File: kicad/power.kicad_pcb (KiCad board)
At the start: 2 copper layers, 84.1 x 61.7 mm, 12 parts, among them J1 Bus_PCI_Express_x1, J2 Conn_01x02_Pin, J6 USB_C_Receptacle_USB2.0_16P

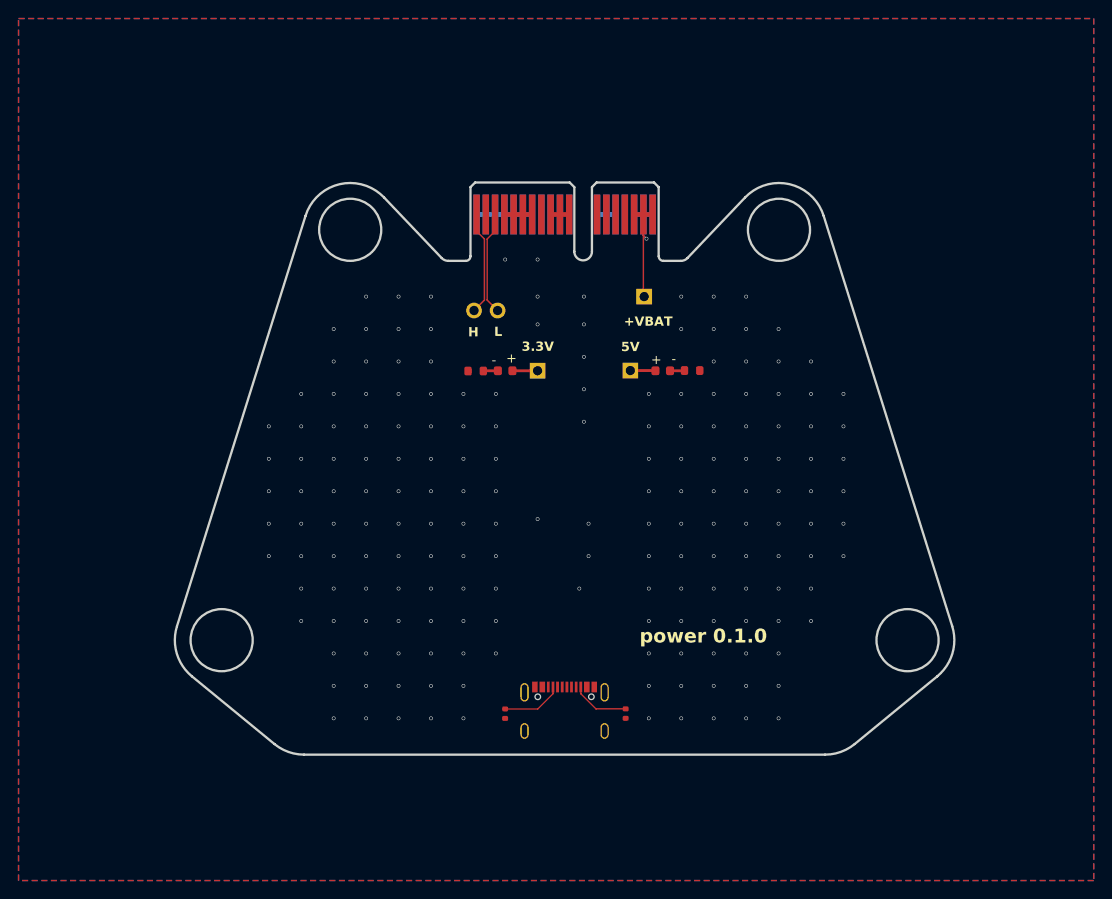
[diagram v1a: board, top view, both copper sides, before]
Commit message: Add MCU and CAN chips
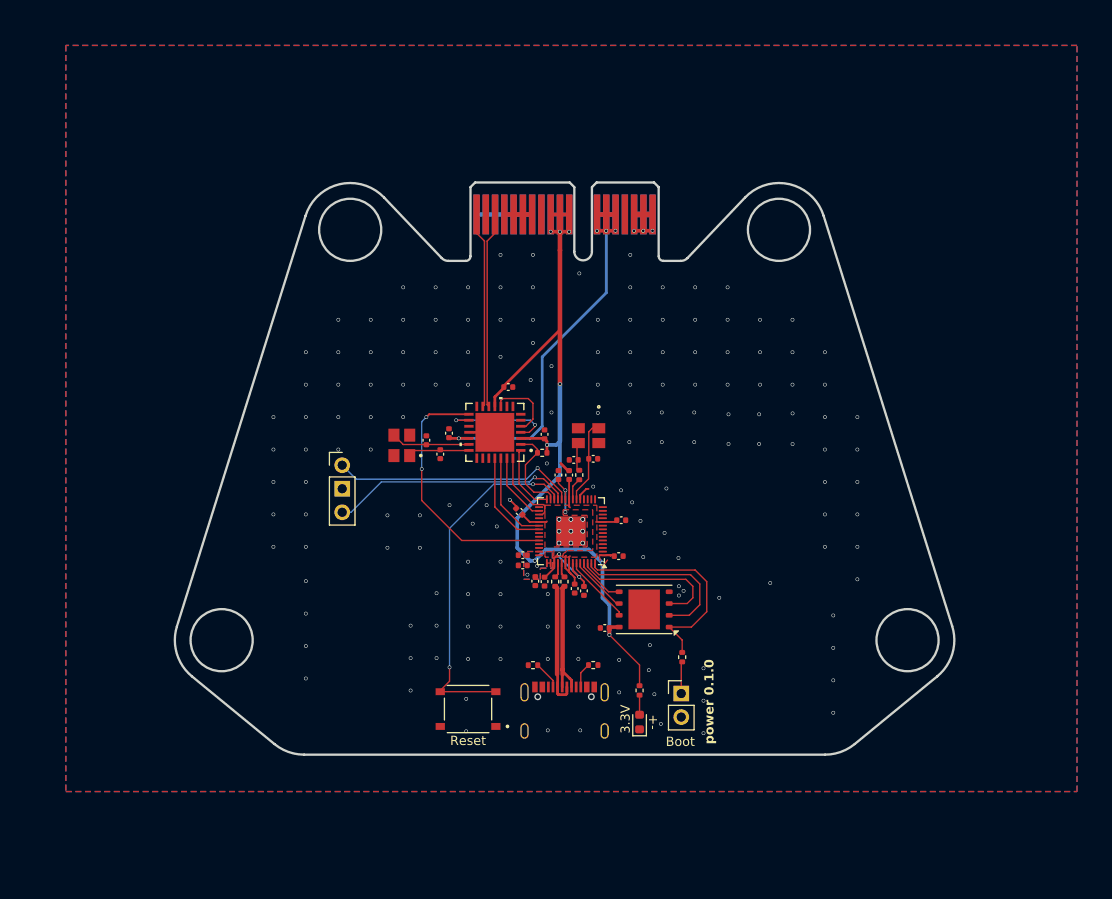
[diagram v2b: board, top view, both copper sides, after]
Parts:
- removed D1, D2: LED, LED_SMD:LED_0603_1608Metric
- removed J2: Conn_01x02_Pin, Connector_PinHeader_2.54mm:PinHeader_1x02_P2.54mm_Vertical
- removed R1, R2: 150, Resistor_SMD:R_0603_1608Metric
- removed TP1, TP2, TP3: TestPoint, Connector_PinHeader_2.54mm:PinHeader_1x01_P2.54mm_Vertical
- added C27: 15p, Capacitor_SMD:C_0402_1005Metric, F.Cu at (149.5, 90.5)
- added C28: 15p, Capacitor_SMD:C_0402_1005Metric, F.Cu at (147.4, 90.6)
- added C29: 100n, Capacitor_SMD:C_0402_1005Metric, F.Cu at (150.8, 108.8)
- added C30: 100n, Capacitor_SMD:C_0402_1005Metric, F.Cu at (140.3, 82.8)
- added C31: 22p, Capacitor_SMD:C_0402_1005Metric, F.Cu at (133.0, 90.0)
- added C32: 100n, Capacitor_SMD:C_0402_1005Metric, F.Cu at (144.2, 87.9)
- added C33: 22p, Capacitor_SMD:C_0402_1005Metric, F.Cu at (131.5, 88.5)
- added C34: 100n, Capacitor_SMD:C_0402_1005Metric, F.Cu at (133.9, 87.7)
- added C35: 100n, Capacitor_SMD:C_0402_1005Metric, F.Cu at (148.5, 104.8)
- added C36: 100n, Capacitor_SMD:C_0402_1005Metric, F.Cu at (145.8, 92.2)
- added C37: 1u, Capacitor_SMD:C_0402_1005Metric, F.Cu at (144.2, 103.8)
- added C38: 100n, Capacitor_SMD:C_0402_1005Metric, F.Cu at (147.5, 104.5)
- added C39: 1u, Capacitor_SMD:C_0402_1005Metric, F.Cu at (143.2, 103.7)
- added C40: 100n, Capacitor_SMD:C_0402_1005Metric, F.Cu at (152.2, 101.0)
- added C41: 100n, Capacitor_SMD:C_0402_1005Metric, F.Cu at (141.5, 96.2)
- added C42: 100n, Capacitor_SMD:C_0402_1005Metric, F.Cu at (152.5, 97.1)
- added C43: 100n, Capacitor_SMD:C_0402_1005Metric, F.Cu at (146.9, 92.3)
- added C44: 100n, Capacitor_SMD:C_0402_1005Metric, F.Cu at (141.9, 100.9)
- added C45: 100n, Capacitor_SMD:C_0402_1005Metric, F.Cu at (141.9, 102.0)
- added D5: LED, LED_SMD:LED_0603_1608Metric, F.Cu at (154.5, 118.9)
- added J3: Conn_01x03, Connector_PinHeader_2.54mm:PinHeader_1x03_P2.54mm_Vertical, F.Cu at (122.4, 91.2)
- added J5: Conn_01x02_Pin, Connector_PinHeader_2.54mm:PinHeader_1x02_P2.54mm_Vertical, F.Cu at (159.0, 115.8)
- added R25: 1k, Resistor_SMD:R_0402_1005Metric, F.Cu at (159.1, 111.9)
- added R26: 1k, Resistor_SMD:R_0402_1005Metric, F.Cu at (148.0, 92.2)
- added R29: 10k, Resistor_SMD:R_0402_1005Metric, F.Cu at (144.0, 89.9)
- added R30: 1 k, Resistor_SMD:R_0402_1005Metric, F.Cu at (154.5, 115.5)
- added R31: 27, Resistor_SMD:R_0402_1005Metric, F.Cu at (146.4, 103.8)
- added R32: 27, Resistor_SMD:R_0402_1005Metric, F.Cu at (145.4, 103.8)
- added S2: TS-1187A-B-A-B, 4in-kicad-library:TS-1187A-B-A-B, F.Cu at (136.0, 117.5)
- added U5: W25Q128JVP, Package_SON:WSON-8-1EP_6x5mm_P1.27mm_EP3.4x4.3mm, F.Cu at (155.0, 106.8)
- added U6: MCP25625T-E/ML, 4in-kicad-library:QFN28_6X6MC_MCH, F.Cu at (138.9, 87.6)
- added U7: RP2040, Package_DFN_QFN:QFN-56-1EP_7x7mm_P0.4mm_EP3.2x3.2mm, F.Cu at (147.1, 98.3)
- added X1: ABM8-272-T3, 4in-kicad-library:ABM8-272-T3_ABR, F.Cu at (149.0, 88.0)
- added Y1: X322516MLB4SI, 4in-kicad-library:X322516MLB4SI, F.Cu at (128.8, 89.1)
- moved R4 6.29 mm to (149.5, 112.8), turned to 0 degrees
- moved R3 6.04 mm to (143.0, 112.8), turned to 0 degrees
- renumbered J1 to J4
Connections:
- net +BAT renamed v_lipo
- J4 pad A1: CANP -> CANH
- J4 pad A3: CANN -> CANL
- J6 pad A1: GND -> LOAD_GND
- J6 pad A12: GND -> LOAD_GND
- J6 pad A4: +5V -> VIN
- J6 pad A9: +5V -> VIN
- J6 pad B1: GND -> LOAD_GND
- J6 pad B12: GND -> LOAD_GND
- J6 pad S1: GND -> LOAD_GND
- R3 pad 1: GND -> LOAD_GND
- R4 pad 2: GND -> LOAD_GND
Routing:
- net +3.3V: track 5.22 -> 112.4 mm, vias 0 -> 10
- net +5V: track 4.67 -> 43.2 mm, vias 0 -> 4
- net /RUN: track 0.00 -> 38.3 mm, vias 0 -> 2
- net (no net): track 0.00 -> 28.7 mm
- net CANSTBY: track 0.00 -> 28.4 mm, vias 0 -> 2
- net /SWCLK: track 0.00 -> 26.7 mm, vias 0 -> 1
- net /SWD: track 0.00 -> 26.2 mm, vias 0 -> 1
- net /QSPI_SS: track 0.00 -> 24.5 mm
- net CANH: track 0.00 -> 21.1 mm
- net CANL: track 0.00 -> 21.1 mm
- net /QSPI_SD1: track 0.00 -> 18.9 mm
- net /QSPI_SD2: track 0.00 -> 16.7 mm
- net +1.1V: track 0.00 -> 14.4 mm, vias 0 -> 4
- net v_lipo: track 18.4 -> 6.00 mm, vias 1 -> 3
- net tx: track 0.00 -> 12.1 mm, vias 0 -> 2
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- added copper zone on F.Cu, net +1.1V
- added copper zone on B.Cu, net +3.3V
- added copper zone on F.Cu, net +3.3V
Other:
- board text added: "+-"
- board text added: "Boot"
- board text added: "Reset"
- board text removed: "+VBAT"
- board text removed: "5V"
- board text removed: "H"
- board text removed: "L"

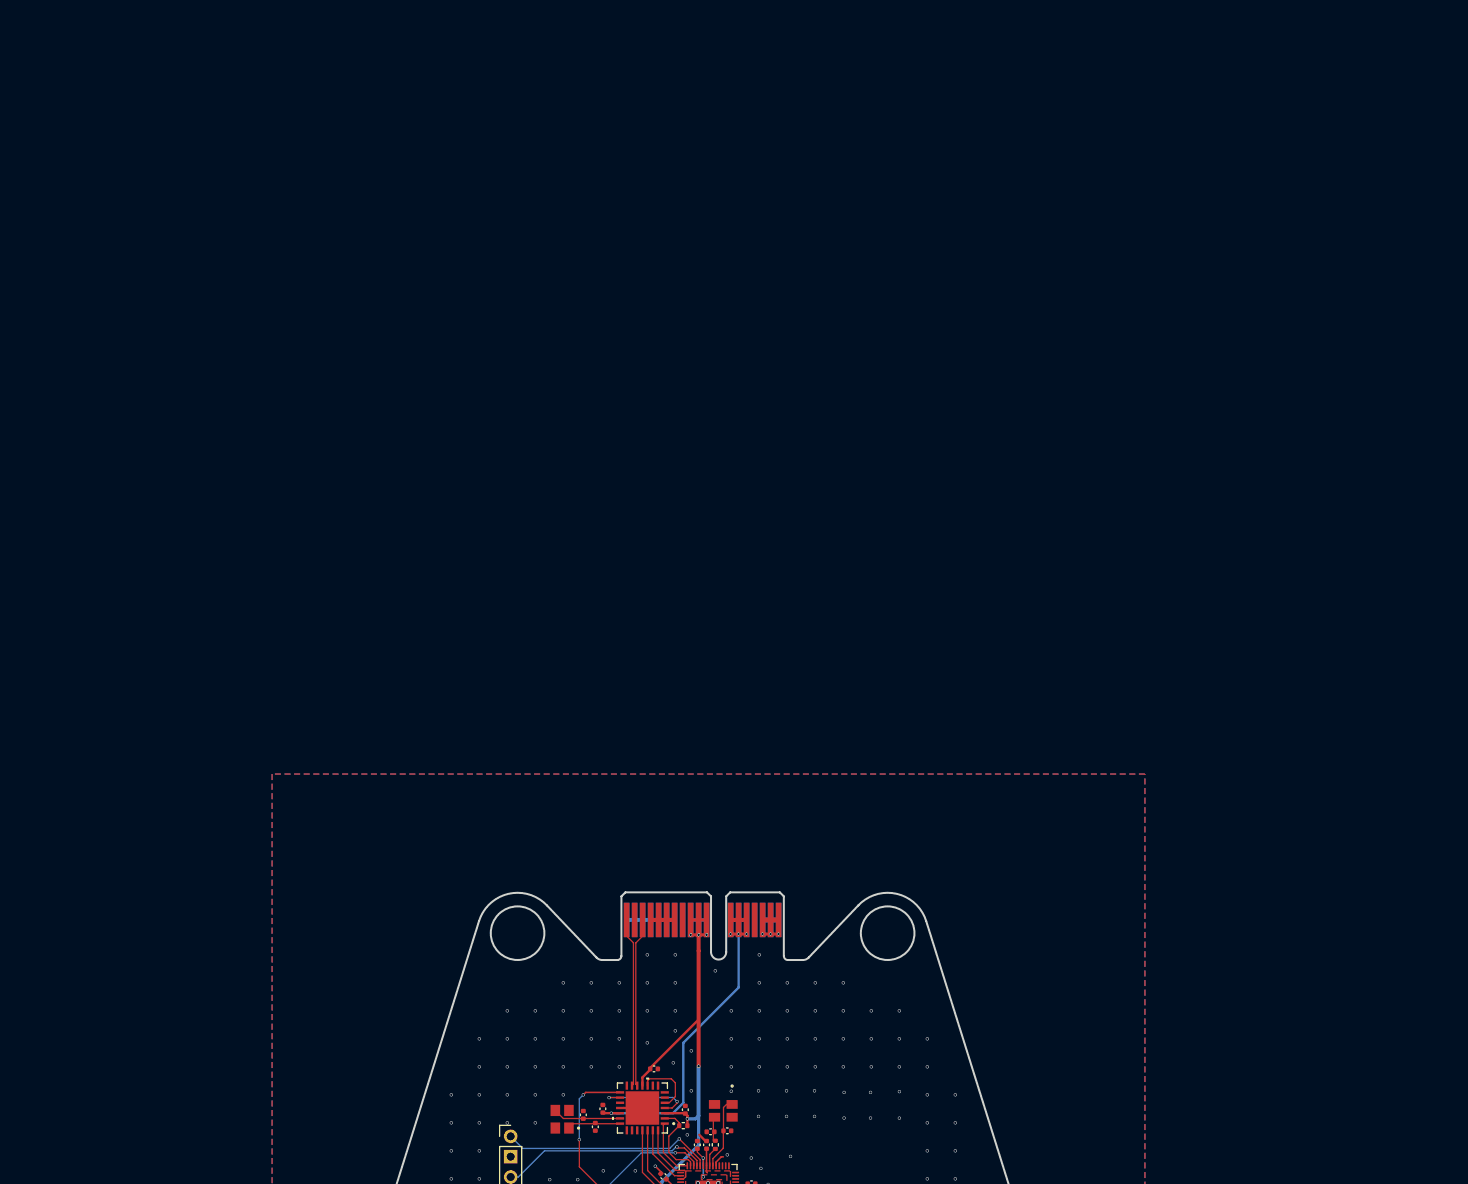
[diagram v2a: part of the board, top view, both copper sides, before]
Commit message: Update component placement
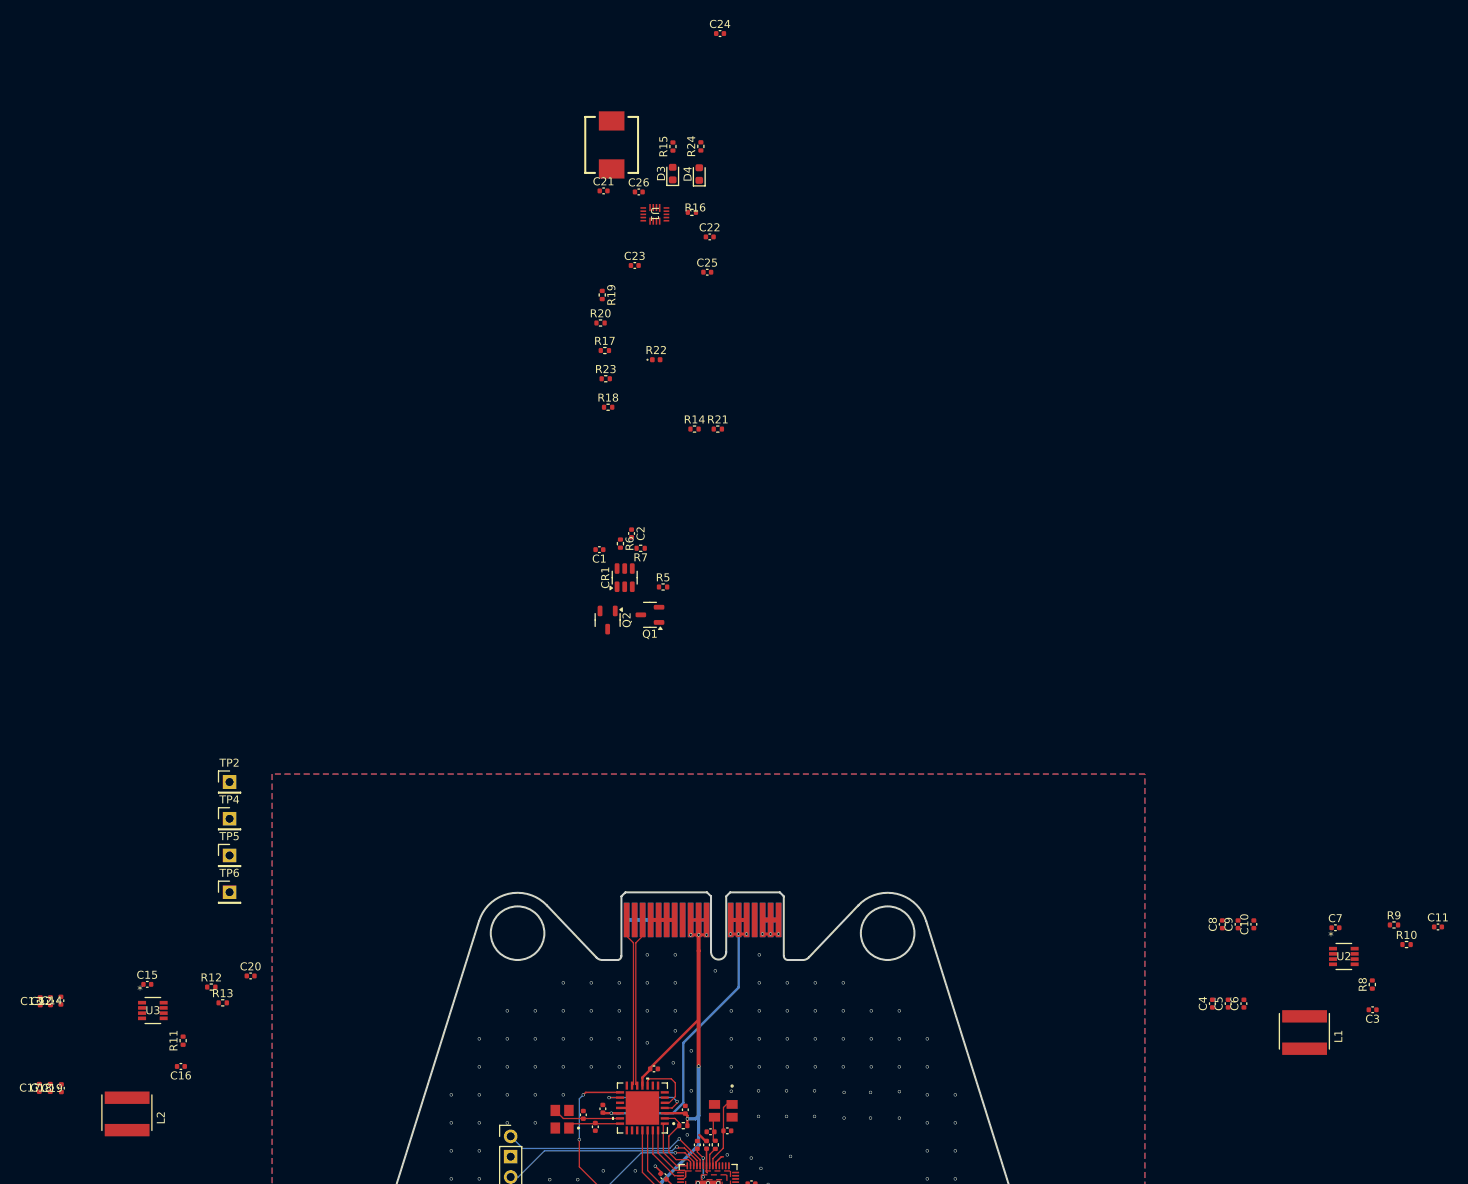
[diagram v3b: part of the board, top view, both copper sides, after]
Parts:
- added C1: 0.1u, Capacitor_SMD:C_0402_1005Metric, F.Cu at (133.5, 17.9)
- added C10: 22u, Capacitor_SMD:C_0402_1005Metric, F.Cu at (215.3, 64.7)
- added C11: 220p, Capacitor_SMD:C_0402_1005Metric, F.Cu at (238.3, 65.0)
- added C12: 22u, Capacitor_SMD:C_0402_1005Metric, F.Cu at (64.9, 74.3)
- added C13: 22u, Capacitor_SMD:C_0402_1005Metric, F.Cu at (63.6, 74.3)
- added C14: 1u, Capacitor_SMD:C_0402_1005Metric, F.Cu at (66.2, 74.2)
- added C15: 1u, Capacitor_SMD:C_0402_1005Metric, F.Cu at (77.0, 72.2)
- added C16: 0.1u, Capacitor_SMD:C_0402_1005Metric, F.Cu at (81.2, 82.5)
- added C17: 22u, Capacitor_SMD:C_0402_1005Metric, F.Cu at (63.5, 85.1)
- added C18: 22u, Capacitor_SMD:C_0402_1005Metric, F.Cu at (64.9, 85.1)
- added C19: 22u, Capacitor_SMD:C_0402_1005Metric, F.Cu at (66.3, 85.2)
- added C2: 0.1u, Capacitor_SMD:C_0402_1005Metric, F.Cu at (137.5, 15.8)
- added C20: 220p, Capacitor_SMD:C_0402_1005Metric, F.Cu at (89.9, 71.1)
- added C21: 10u, Capacitor_SMD:C_0402_1005Metric, F.Cu at (134.0, -27.0)
- added C22: 22u, Capacitor_SMD:C_0402_1005Metric, F.Cu at (147.3, -21.2)
- added C23: 1u, Capacitor_SMD:C_0402_1005Metric, F.Cu at (137.9, -17.7)
- added C24: 10u, Capacitor_SMD:C_0402_1005Metric, F.Cu at (148.6, -46.7)
- added C25: 22u, Capacitor_SMD:C_0402_1005Metric, F.Cu at (147.0, -16.8)
- added C26: 100n, Capacitor_SMD:C_0402_1005Metric, F.Cu at (138.4, -26.9)
- added C3: 0.1u, Capacitor_SMD:C_0402_1005Metric, F.Cu at (230.2, 75.4)
- added C4: 22u, Capacitor_SMD:C_0402_1005Metric, F.Cu at (210.1, 74.6)
- added C5: 22u, Capacitor_SMD:C_0402_1005Metric, F.Cu at (212.1, 74.6)
- added C6: 22u, Capacitor_SMD:C_0402_1005Metric, F.Cu at (214.1, 74.6)
- added C7: 1u, Capacitor_SMD:C_0402_1005Metric, F.Cu at (225.5, 65.1)
- added C8: 1u, Capacitor_SMD:C_0402_1005Metric, F.Cu at (211.4, 64.7)
- added C9: 22u, Capacitor_SMD:C_0402_1005Metric, F.Cu at (213.3, 64.7)
- added CR1: S-8252AAL-M6T1U, Package_TO_SOT_SMD:SOT-23-6, F.Cu at (136.7, 21.4)
- added D3: LED, LED_SMD:LED_0603_1608Metric, F.Cu at (142.7, -29.2)
- added D4: LED, LED_SMD:LED_0603_1608Metric, F.Cu at (146.0, -29.1)
- added L1: MPL-AL6050-3R3, POWERLIB:2-SMD, F.Cu at (221.7, 78.1)
- added L2: MPL-AL6050-2R2, POWERLIB:2-SMD, F.Cu at (74.5, 88.2)
- added L3: 1.5uH, POWERLIB:IND-SMD_L7.0-W6.6, F.Cu at (135.0, -32.7)
- added Q1: AO3400A, Package_TO_SOT_SMD:SOT-23-3, F.Cu at (139.8, 26.0)
- added Q2: AO3400A, Package_TO_SOT_SMD:SOT-23-3, F.Cu at (134.5, 26.6)
- added R10: 100k, Resistor_SMD:R_0402_1005Metric, F.Cu at (234.4, 67.2)
- added R11: 10R, Resistor_SMD:R_0402_1005Metric, F.Cu at (81.5, 79.2)
- added R12: 22.1k, Resistor_SMD:R_0402_1005Metric, F.Cu at (85.0, 72.5)
- added R13: 100k, Resistor_SMD:R_0402_1005Metric, F.Cu at (86.4, 74.5)
- added R14: 5.5k, Resistor_SMD:R_0402_1005Metric, F.Cu at (145.4, 2.78)
- added R15: 100R, Resistor_SMD:R_0402_1005Metric, F.Cu at (142.7, -32.5)
- added R16: 30k, Resistor_SMD:R_0402_1005Metric, F.Cu at (145.1, -24.3)
- added R17: 60R, Resistor_SMD:R_0402_1005Metric, F.Cu at (134.2, -7.04)
- added R18: 8k, Resistor_SMD:R_0402_1005Metric, F.Cu at (134.6, 0.05)
- added R19: 12.6k, Resistor_SMD:R_0402_1005Metric, F.Cu at (133.9, -14.0)
- added R20: 3.6k, Resistor_SMD:R_0402_1005Metric, F.Cu at (133.7, -10.5)
- added R21: 2k, Resistor_SMD:R_0402_1005Metric, F.Cu at (148.3, 2.78)
- added R22: NTCG103JF103FT1, Diode_SMD:D_0402_1005Metric, F.Cu at (140.6, -5.89)
- added R23: 60R, Resistor_SMD:R_0402_1005Metric, F.Cu at (134.3, -3.51)
- added R24: 100R, Resistor_SMD:R_0402_1005Metric, F.Cu at (146.2, -32.6)
- added R5: 2k, Resistor_SMD:R_0402_1005Metric, F.Cu at (141.5, 22.5)
- added R6: 470R, Resistor_SMD:R_0402_1005Metric, F.Cu at (136.1, 17.1)
- added R7: 470R, Resistor_SMD:R_0402_1005Metric, F.Cu at (138.7, 17.7)
- added R8: 10R, Resistor_SMD:R_0402_1005Metric, F.Cu at (230.1, 72.2)
- added R9: 13.7k, Resistor_SMD:R_0402_1005Metric, F.Cu at (232.8, 64.8)
- added TP2: TestPoint, Connector_PinHeader_2.54mm:PinHeader_1x01_P2.54mm_Vertical, F.Cu at (87.3, 46.9)
- added TP4: TestPoint, Connector_PinHeader_2.54mm:PinHeader_1x01_P2.54mm_Vertical, F.Cu at (87.3, 51.5)
- added TP5: TestPoint, Connector_PinHeader_2.54mm:PinHeader_1x01_P2.54mm_Vertical, F.Cu at (87.3, 56.1)
- added TP6: TestPoint, Connector_PinHeader_2.54mm:PinHeader_1x01_P2.54mm_Vertical, F.Cu at (87.3, 60.7)
- added U1: MP2672GD-0000-Z, POWERLIB:QFN-18_2MMx3MM_MP2672_MNP_MPS, F.Cu at (140.4, -24.1)
- added U2: MP2236CGJ-P, POWERLIB:TSOT23-8_MP2236C_MNP, F.Cu at (226.6, 68.7)
- added U3: MP2236CGJ-P, POWERLIB:TSOT23-8_MP2236C_MNP, F.Cu at (77.7, 75.5)
- renumbered J3 to J7
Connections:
- J4 pad A1: CANH -> CANP
- J4 pad A16: v_lipo -> unconnected-(J4-PERp0-PadA16)
- J4 pad A17: v_lipo -> unconnected-(J4-PERn0-PadA17)
- J4 pad A18: v_lipo -> unconnected-(J4-GND-PadA18)
- J4 pad A3: CANL -> CANN
- J4 pad B16: v_lipo -> unconnected-(J4-GND-PadB16)
- J4 pad B17: v_lipo -> unconnected-(J4-~{PRSNT2}-PadB17)
- J4 pad B18: v_lipo -> unconnected-(J4-GND-PadB18)
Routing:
- net CANP: track 0.00 -> 21.1 mm
- net CANH: track 21.1 -> 0.00 mm
- net CANN: track 0.00 -> 21.1 mm
- net CANL: track 21.1 -> 0.00 mm
- net v_lipo: track 6.00 -> 0.00 mm, vias 3 -> 0
- net (no net): track 28.7 -> 34.7 mm, vias 0 -> 3
